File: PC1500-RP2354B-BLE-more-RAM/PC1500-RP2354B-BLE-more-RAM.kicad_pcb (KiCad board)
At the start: 8 copper layers, 31.9 x 43 mm, 41 parts, among them J1 microSD, J2 USB-C (programming/debug), J3 PC-1500 40-pin cartridge slot, J5 PC1500_SENSE_JUMPER, J7 SWD_I2C_HEADER, SW1 BOOTSEL, U1 RP2354B, U10 TCA9406DCUR, U2 AS6C1008-55TINL, U3 SLG46826V, U4 AP2112K-3.3, U5 MCP6541T-I/LT, U8 BGM220SC22WGA2, U9 SLG46826V, X1 12MHz (Abracon ABM8-272-T3)

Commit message: More-RAM card: BLE_MODULE_WAKE (GPIO27 to BGM220S PB03); I2C pull-ups
- BLE_MODULE_WAKE: the MCU-to-module wake (an EM4 wake pin on the
  module), lost in the bus rewire. Pads updated; routing left for later.
- R25/R26: 1.5K pull-ups from SDA/SCL to +3V3.

Co-Authored-By: Claude Opus 5.5 <noreply@anthropic.com>
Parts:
- added R25: 1.5K, Resistor_SMD:R_0201_0603Metric, F.Cu at (159.1, 71.8)
- added R26: 1.5K, Resistor_SMD:R_0201_0603Metric, F.Cu at (158.3, 71.8)
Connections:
- J7 pad 1: SCL_GP -> unconnected-(J7-Pin_1-Pad1)
- J7 pad 3: SDA_GP -> unconnected-(J7-Pin_3-Pad3)
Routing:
- net SCL: track 16.3 -> 17.6 mm
- net +3V3: track 36.0 -> 36.8 mm, vias 18 -> 19

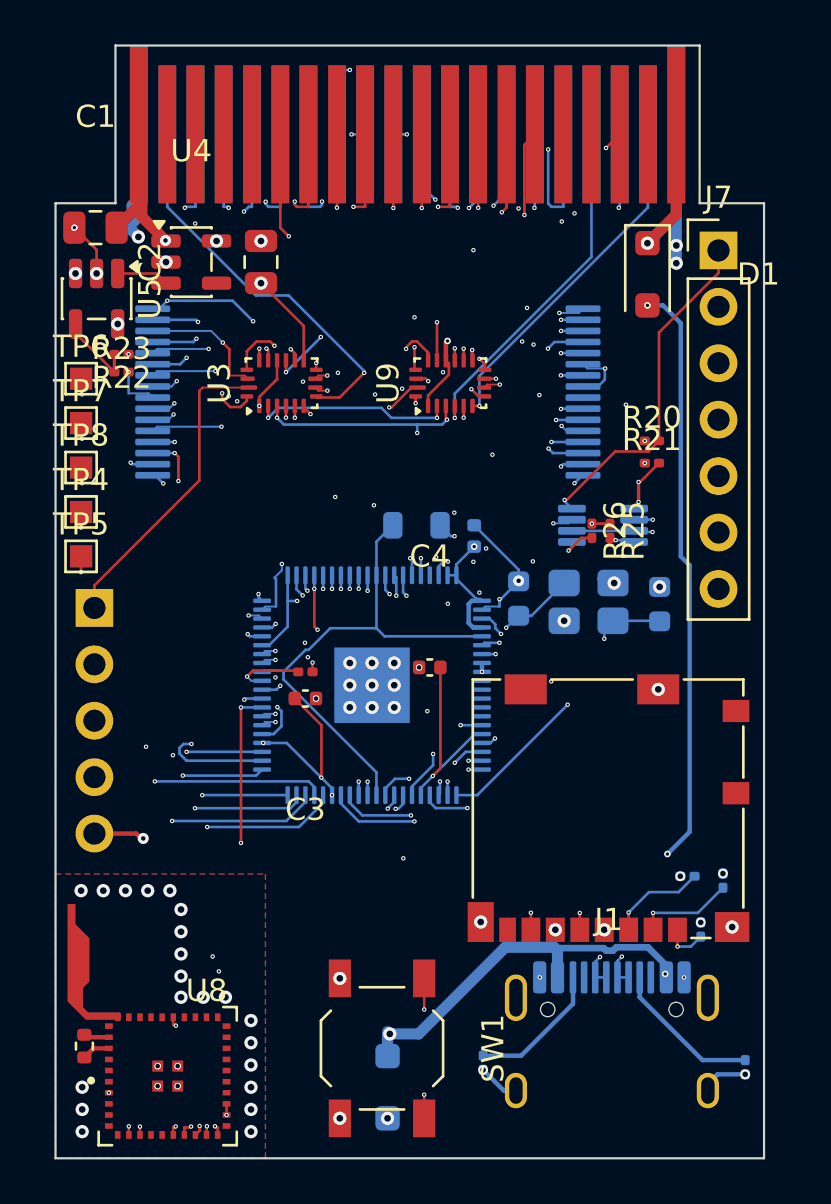
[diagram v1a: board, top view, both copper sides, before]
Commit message: More-RAM card: GP2 INHIBIT/MCU_READY/TRIG_WR_SYS, test points, USB 27R, decoupling, Abracon L2; placed and routed
Schematic:
- INHIBIT from GP2 (U9) IO10; U9 IO14 = MCU_READY -> GPIO25; U9 IO12 =
  TRIG_WR_SYS (7000-7FFF write trigger) -> GPIO24.
- Test points: TP4 on GPIO46; TP9 GP1_IO6, TP10 GP2_IO13, TP11 card-edge PU.
- USB-C D+/D- pairing fixed; R27/R28 27R series resistors.
- Decoupling per Raspberry Pi's "Hardware design with RP2350": 100nF per
  RP2354B power pin, 4.7uF on VREG_VIN and DVDD, R29 33R + C27 4.7uF on
  VREG_AVDD (FLG5). One 100nF per GreenPAK at VDD, two on the SRAM.
- L2 = Abracon AOTA-B201610S3R3-101-T (LCSC C42411119) on a new
  Sharp-PC-Footprints:L_Abracon_AOTA-B201610 footprint, generated by
  tools/gen_fp_abracon_aota_b201610.py from Abracon's land pattern.
- TP values follow their nets.

PCB: new parts placed and routed; DVDD 4.7uF moved next to L2's output;
XOUT straightened; reference designators restored to match the schematic
(silkscreen labels kept as Value fields / ${REFERENCE} texts). DRC: 0
unconnected, schematic parity only the PWR_FLAGs; remaining clearance
errors are the J1 shell vias (expected, see DESIGN_DECISIONS.md).
Design rules updated in the .kicad_pro.

Co-Authored-By: Claude Opus 5.5 <noreply@anthropic.com>
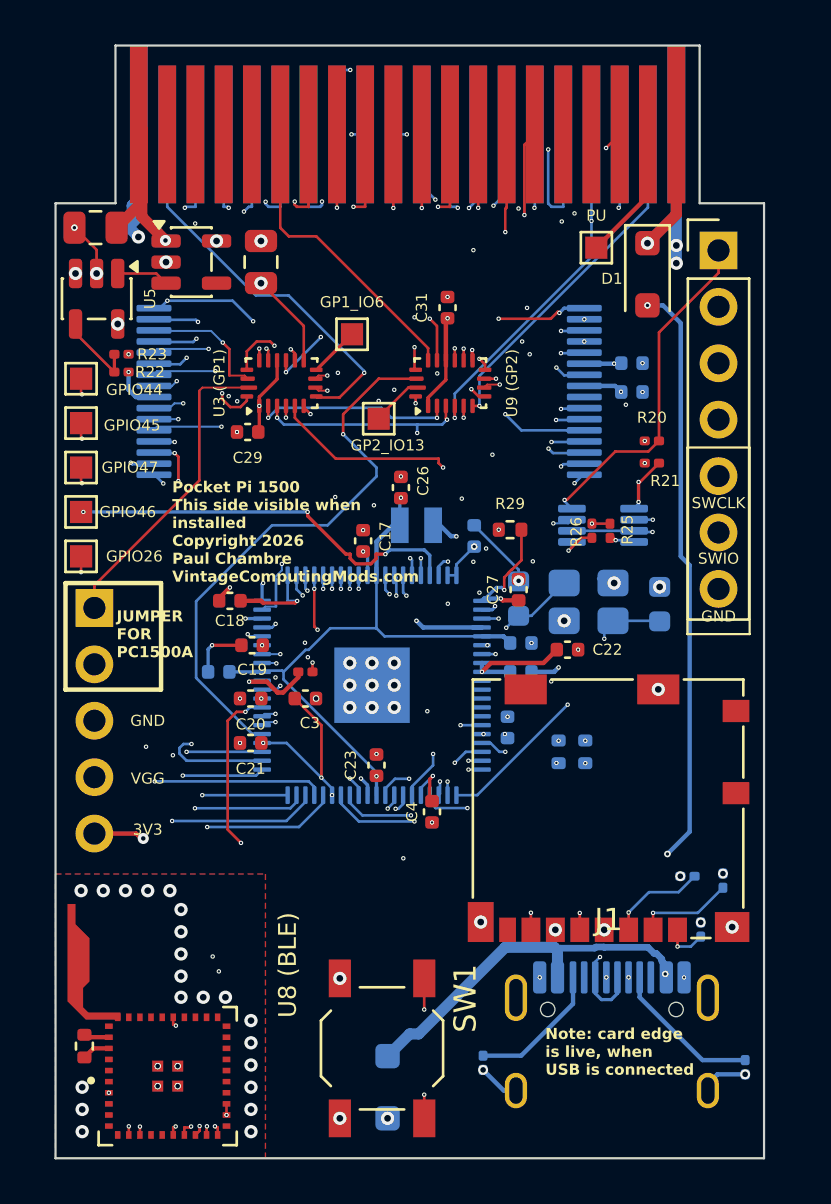
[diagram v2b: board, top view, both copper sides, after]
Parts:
- added C15: 100nF, Capacitor_SMD:C_0402_1005Metric, B.Cu at (155.1, 78.2)
- added C16: 100nF, Capacitor_SMD:C_0402_1005Metric, B.Cu at (154.5, 80.7)
- added C17: 100nF, Capacitor_SMD:C_0402_1005Metric, F.Cu at (148.0, 72.3)
- added C18: 100nF, Capacitor_SMD:C_0402_1005Metric, F.Cu at (142.0, 75.0)
- added C19: 100nF, Capacitor_SMD:C_0402_1005Metric, F.Cu at (143.0, 77.0)
- added C20: 100nF, Capacitor_SMD:C_0402_1005Metric, F.Cu at (142.9, 79.4)
- added C21: 100nF, Capacitor_SMD:C_0402_1005Metric, F.Cu at (142.9, 81.4)
- added C22: 4.7uF, Capacitor_SMD:C_0402_1005Metric, F.Cu at (157.2, 77.2)
- added C23: 100nF, Capacitor_SMD:C_0402_1005Metric, F.Cu at (148.6, 82.4)
- added C24: 100nF, Capacitor_SMD:C_0402_1005Metric, B.Cu at (155.1, 76.9)
- added C25: 100nF, Capacitor_SMD:C_0402_1005Metric, B.Cu at (141.5, 78.2)
- added C26: 4.7uF, Capacitor_SMD:C_0402_1005Metric, F.Cu at (149.7, 69.9)
- added C27: 4.7uF, Capacitor_SMD:C_0402_1005Metric, F.Cu at (155.0, 74.5)
- added C29: 100nF, Capacitor_SMD:C_0402_1005Metric, F.Cu at (142.8, 67.4)
- added C30: 100nF, Capacitor_SMD:C_0402_1005Metric, B.Cu at (160.1, 65.6)
- added C31: 100nF, Capacitor_SMD:C_0402_1005Metric, F.Cu at (151.8, 61.8)
- added C32: 100nF, Capacitor_SMD:C_0402_1005Metric, B.Cu at (160.1, 64.3)
- added R27: 27R, Resistor_SMD:R_0402_1005Metric, B.Cu at (156.8, 81.8)
- added R28: 27R, Resistor_SMD:R_0402_1005Metric, B.Cu at (158.0, 81.8)
- added R29: 33R, Resistor_SMD:R_0402_1005Metric, F.Cu at (154.6, 71.8)
- added TP10: GP2_IO13, TestPoint:TestPoint_Pad_1.0x1.0mm, F.Cu at (148.7, 66.8)
- added TP11: PU, TestPoint:TestPoint_Pad_1.0x1.0mm, F.Cu at (158.5, 59.1)
- added TP9: GP1_IO6, TestPoint:TestPoint_Pad_1.0x1.0mm, F.Cu at (147.5, 63.0)
- L2: value 1uH -> 3.3uH (Abracon AOTA-B201610S3R3-101-T); footprint Inductor_SMD:L_0805_2012Metric -> Sharp-PC-Footprints:L_Abracon_AOTA-B201610
- TP4: value GPIO19 -> GPIO46
- TP5: value GPIO20 -> GPIO26
- TP8: value GPIO34 -> GPIO47
- moved C4 6.50 mm to (151.1, 84.5), turned to 90 degrees
- moved U2 0.06 mm to (148.3, 65.6)
- turned L2 to 0 degrees
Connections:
- net GREENPAK2_IO14 renamed MCU_READY
- J2 pad A6: USB_DM -> USB_C_DP
- J2 pad A7: USB_DP -> USB_C_DM
- J2 pad B6: USB_DP -> USB_C_DP
- J2 pad B7: USB_DM -> USB_C_DM
- J7 pad 1: unconnected-(J7-Pin_1-Pad1) -> SCL_GP
- J7 pad 3: unconnected-(J7-Pin_3-Pad3) -> SDA_GP
- TP4 pad 1: GPIO24 -> GPIO46
- U1 pad 25: GPIO24 -> TRIG_WR_SYS
- U1 pad 61: +3V3 -> VREG_AVDD
- U2 pad 1: SRAM_A11 -> AD11
- U2 pad 12: SRAM_A12 -> AD12
- U2 pad 4: SRAM_A13 -> AD13
- U3 pad 10: SRAM_A11 -> GP1_IO6
- U3 pad 12: SRAM_A12 -> SRAM_A14
- U3 pad 13: SRAM_A13 -> SRAM_A15
- U3 pad 15: SRAM_A14 -> SRAM_A16
- U9 pad 1: VCC -> VGG
- U9 pad 14: VCC -> VGG
- U9 pad 16: SRAM_A15 -> INHIBIT
- U9 pad 18: SRAM_A16 -> TRIG_WR_SYS
- U9 pad 19: INHIBIT -> GP2_IO13
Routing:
- net TRIG_WR_SYS: track 0.00 -> 25.3 mm, vias 0 -> 1
- net GPIO46: track 0.00 -> 18.2 mm, vias 0 -> 3
- net SRAM_A11: track 16.3 -> 0.00 mm, vias 3 -> 0
- net SRAM_A12: track 16.2 -> 0.00 mm, vias 2 -> 0
- net SRAM_A13: track 15.5 -> 0.00 mm, vias 3 -> 0
- net GPIO24: track 14.8 -> 0.00 mm, vias 2 -> 0
- net USB_C_DP: track 0.00 -> 13.2 mm, vias 0 -> 2
- net USB_DP: track 18.8 -> 5.80 mm
- net USB_DM: track 18.8 -> 6.83 mm
- net USB_C_DM: track 0.00 -> 11.5 mm, vias 0 -> 3
- net SRAM_A16: track 8.07 -> 18.5 mm, vias 2 -> 3
- net AD12: track 48.8 -> 56.1 mm, vias 5 -> 6
- net VGG: track 16.8 -> 23.8 mm, vias 9 -> 11
- net VREG_AVDD: track 0.00 -> 6.07 mm, vias 0 -> 2
- net PU: track 0.00 -> 6.06 mm
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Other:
- board text added: "3V3"
- board text added: "GND"
- board text added: "JUMPER FOR PC1500A"
- board text added: "Note: card edge is live, when USB is connected"
- board text added: "Pocket Pi 1500 This side visible when installed Copyright 2026 Paul Chambre VintageComputingMods.com"
- board text added: "SWCLK"
- board text added: "SWIO"
- board text added: "This side NOT visible when installed"
- board text added: "VGG"
